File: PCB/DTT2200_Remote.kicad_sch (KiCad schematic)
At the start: 12 parts, among them J1 Mini-DIN-6, SW1 RotaryEncoder_Switch, SW2 RotaryEncoder, SW3 SW_SPDT, U1 ESP32-C3-WROOM-02, U2 AD5262BRUZ50

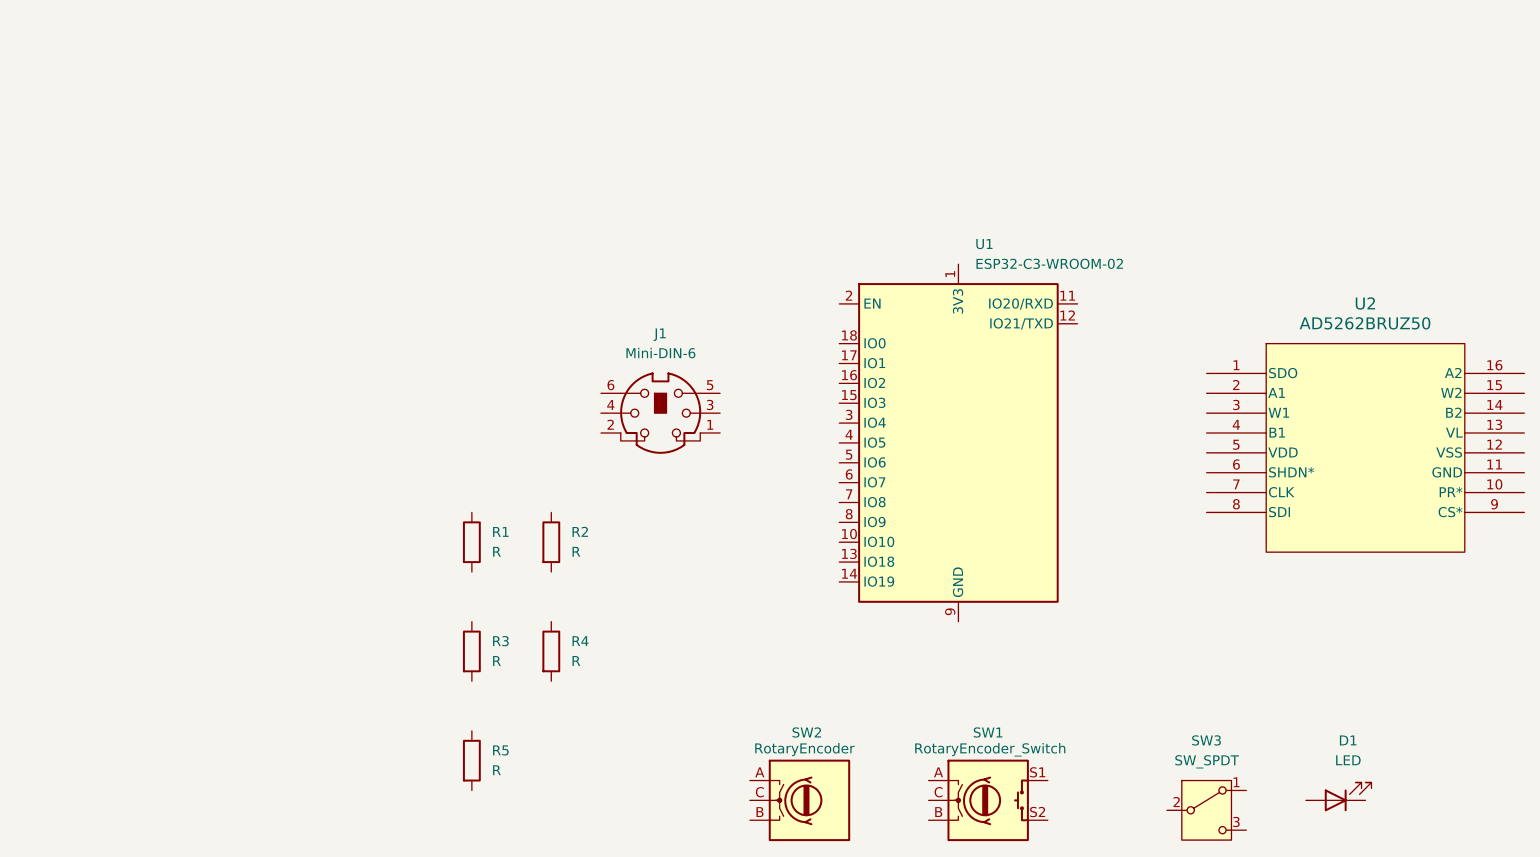
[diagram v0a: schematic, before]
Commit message: wired the digital pot
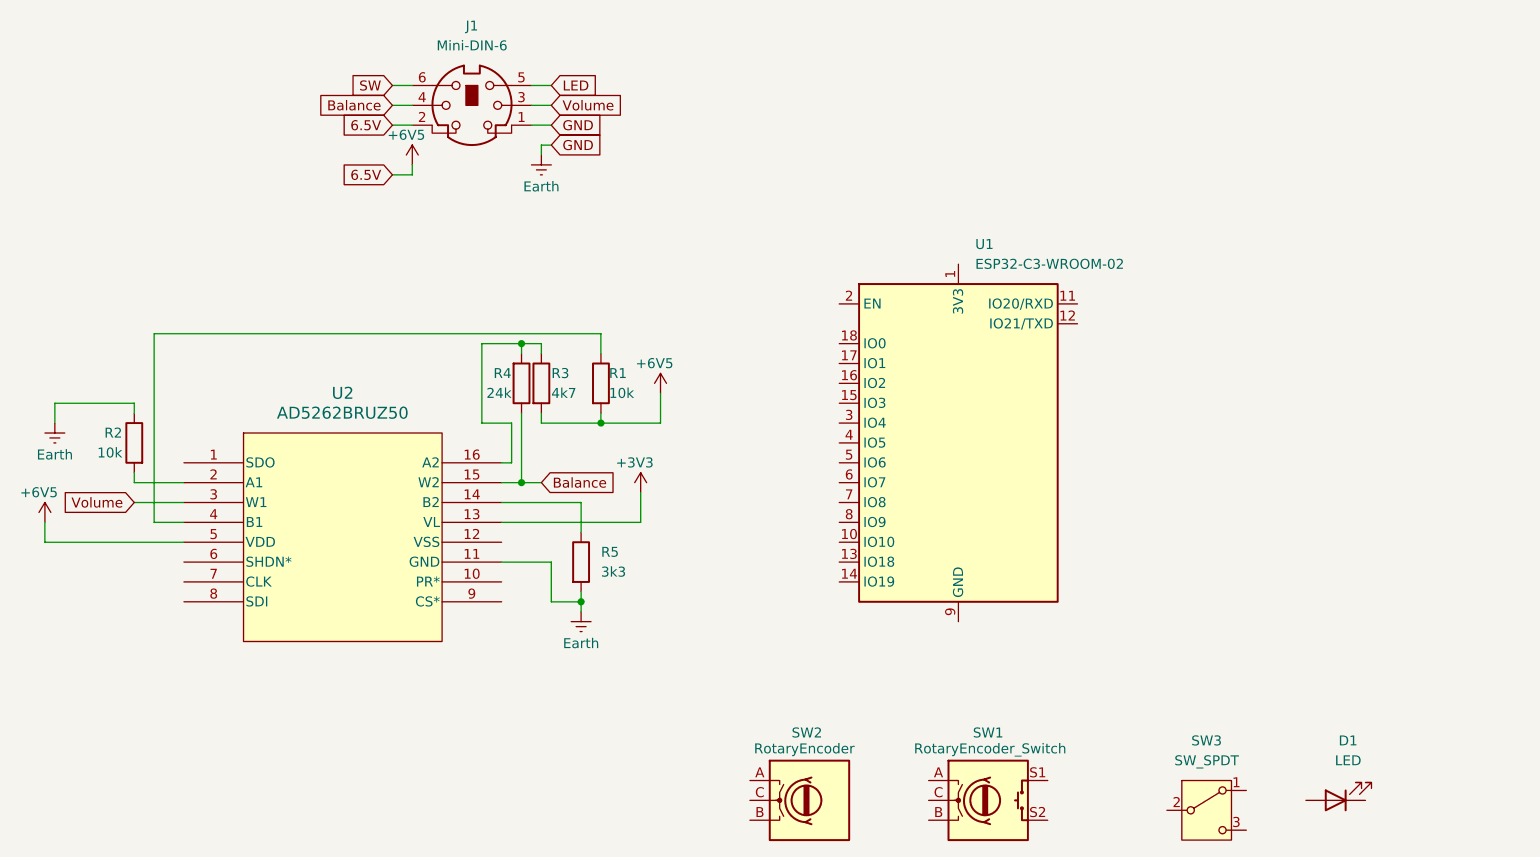
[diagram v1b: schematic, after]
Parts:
- R1, R2: value R -> 10k
- R3: value R -> 4k7
- R4: value R -> 24k
- R5: value R -> 3k3
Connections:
- net Earth: now reaches J1.1
- net Earth: now also R2.1, R5.2, U2.11 (GND)
- net +6V5: now reaches J1.2
- net +6V5: now also R1.2, R3.2, U2.5 (VDD)
- net Volume: now reaches J1.3
- net Volume: now also U2.3 (W1)
- net Balance: now reaches J1.4
- net Balance: now also R4.1, U2.15 (W2)
- net LED: now reaches J1.5
- net SW: now reaches J1.6
- net at R1.1: now also U2.4 (B1)
- net at R4.2: now also R3.1, U2.16 (A2)
- net at R2.2: now also U2.2 (A1)
- net at R5.1: now also U2.14 (B2)
- net +3V3: now reaches U2.13 (VL)
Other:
- moved on the sheet: J1, R1, R2, R3, R4, R5, U2
